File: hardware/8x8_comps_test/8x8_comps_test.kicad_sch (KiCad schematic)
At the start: 10 parts

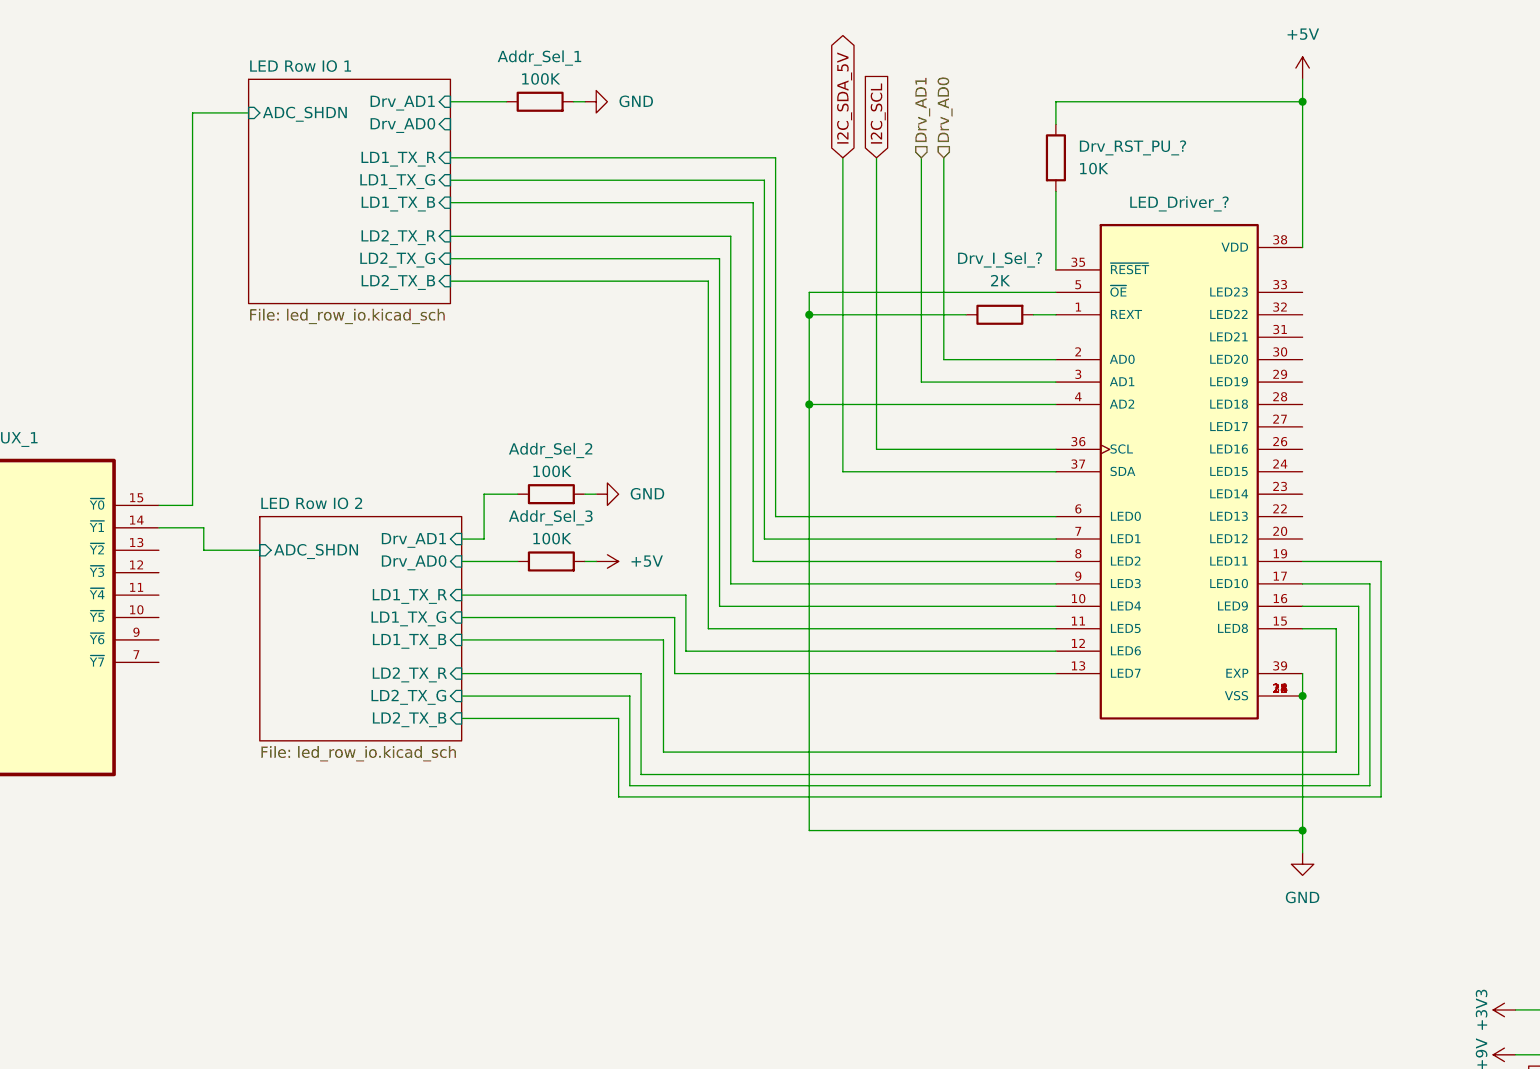
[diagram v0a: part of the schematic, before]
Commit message: Added test Schematic and PCB
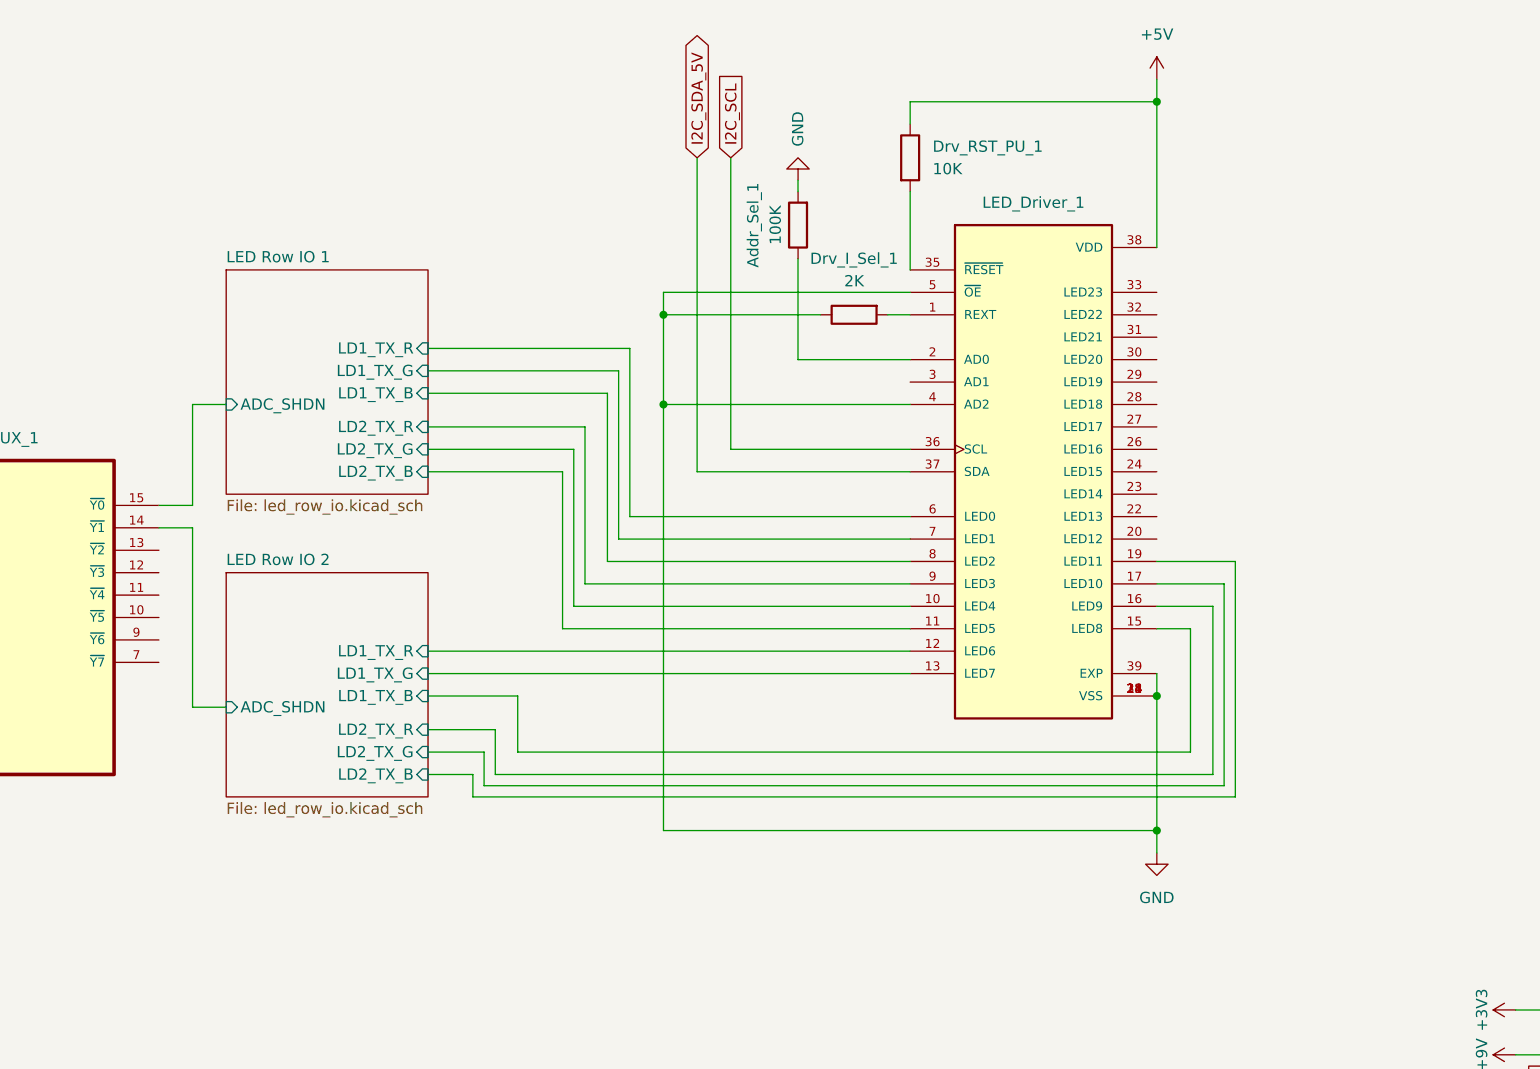
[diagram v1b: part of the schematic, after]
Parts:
- removed Addr_Sel_2, Addr_Sel_3: 100K, Resistor_THT:R_Axial_DIN0207_L6.3mm_D2.5mm_P7.62mm_Horizontal, symbol Device:R
- gave numbers to parts that had none: 3
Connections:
- net LED Row IO 1/Drv_AD1 is gone; now on an unnamed net: Addr_Sel_1.1
- net Drv_AD0: no longer names the net of LED_Driver_1.2 (AD0)
- net Drv_AD1: no longer names the net of LED_Driver_1.3 (AD1)
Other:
- sheet LED Row IO 1 ports: added none; removed Drv_AD0, Drv_AD1
- sheet LED Row IO 2 ports: added none; removed Drv_AD0, Drv_AD1
- moved on the sheet: Addr_Sel_1, Drv_I_Sel_1, Drv_RST_PU_1, LED_Driver_1

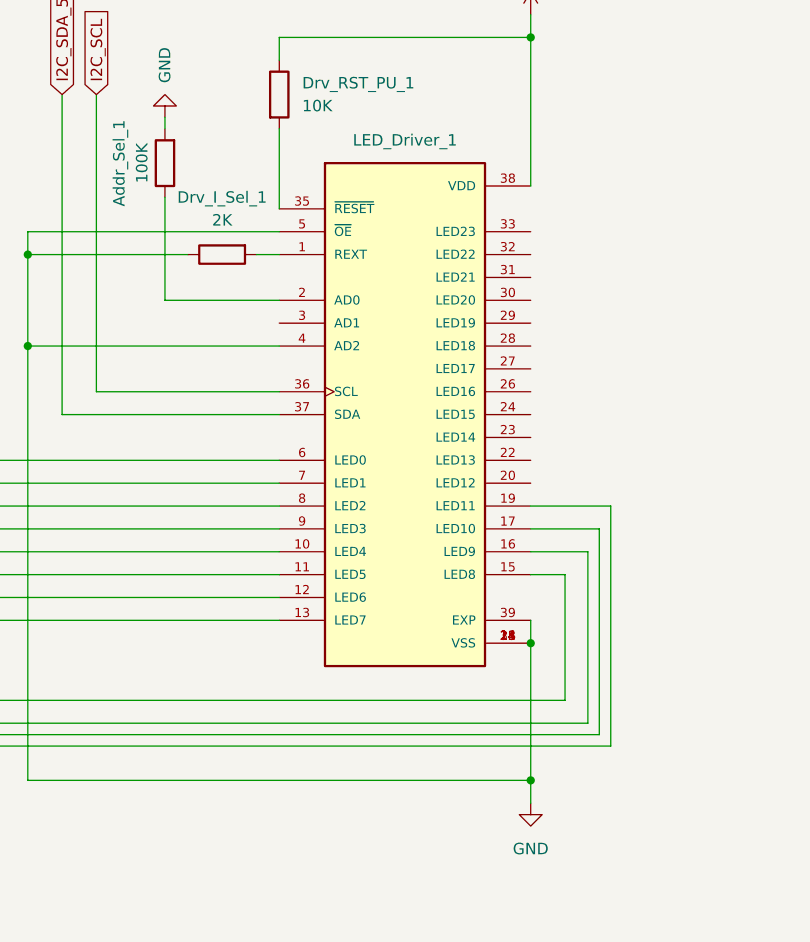
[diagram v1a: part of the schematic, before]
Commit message: Updated Footprints
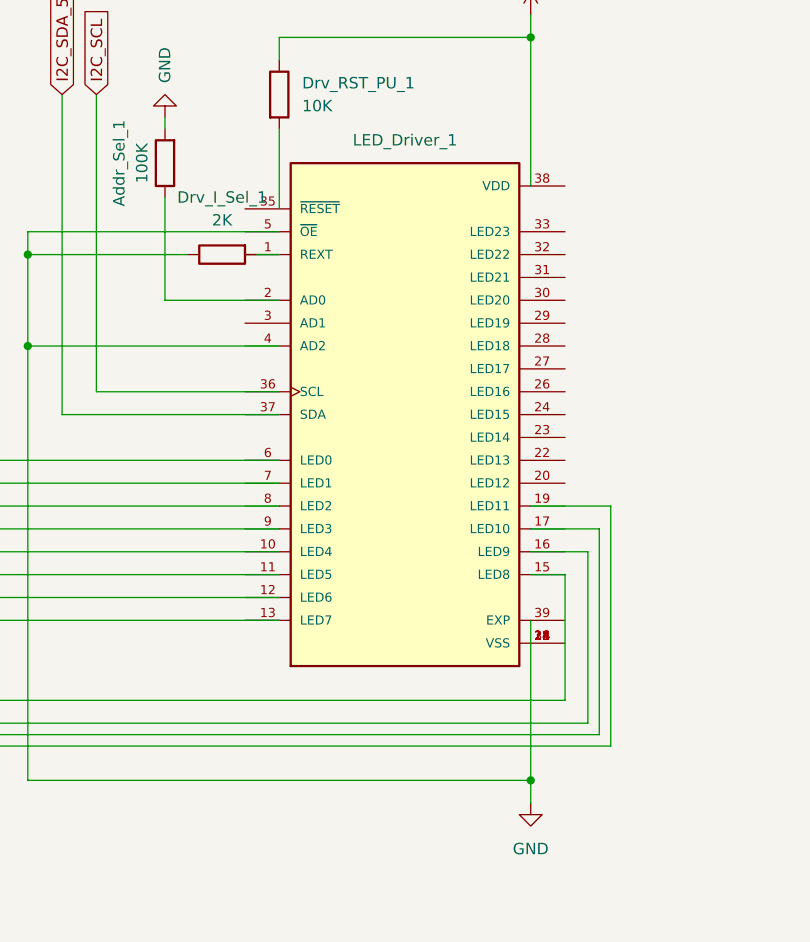
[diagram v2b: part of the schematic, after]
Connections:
- net +5V: no longer LED_Driver_1.38 (VDD)
- net GND: no longer LED_Driver_1.14 (VSS), LED_Driver_1.18 (VSS), LED_Driver_1.21 (VSS), LED_Driver_1.25 (VSS), LED_Driver_1.34 (VSS), LED_Driver_1.39 (EXP), LED_Driver_1.4 (AD2), LED_Driver_1.5 (~{OE})
- net I2C_SCL: no longer LED_Driver_1.36 (SCL)
- net I2C_SDA_5V: no longer LED_Driver_1.37 (SDA)
- net LED Row IO 1/LD1_TX_B: no longer LED_Driver_1.8 (LED2)
- net LED Row IO 1/LD1_TX_G: no longer LED_Driver_1.7 (LED1)
- net LED Row IO 1/LD1_TX_R: no longer LED_Driver_1.6 (LED0)
- net LED Row IO 1/LD2_TX_B: no longer LED_Driver_1.11 (LED5)
- net LED Row IO 1/LD2_TX_G: no longer LED_Driver_1.10 (LED4)
- net LED Row IO 1/LD2_TX_R: no longer LED_Driver_1.9 (LED3)
- net LED Row IO 2/LD1_TX_G: no longer LED_Driver_1.13 (LED7)
- net LED Row IO 2/LD1_TX_R: no longer LED_Driver_1.12 (LED6)
- net LED Row IO 2/LD2_TX_B: no longer LED_Driver_1.19 (LED11)
- net LED Row IO 2/LD2_TX_G: no longer LED_Driver_1.17 (LED10)
- net LED Row IO 2/LD2_TX_R: no longer LED_Driver_1.16 (LED9)
- net at LED_Driver_1.1 (REXT): no longer Drv_I_Sel_1.2
- net at LED_Driver_1.2 (AD0): no longer Addr_Sel_1.1
- net at LED_Driver_1.35 (~{RESET}): no longer Drv_RST_PU_1.2
- new net: LED_Driver_1.14 (VSS), LED_Driver_1.18 (VSS), LED_Driver_1.21 (VSS), LED_Driver_1.25 (VSS), LED_Driver_1.34 (VSS)
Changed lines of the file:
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@@
   (junction (at 185.42 104.14) (diameter 0) (color 0 0 0 0)
   )
-  (junction (at 185.42 88.9) (diameter 0) (color 0 0 0 0)
-  )
   (junction (at 185.42 21.59) (diameter 0) (color 0 0 0 0)
   )
@@
     (stroke (width 0) (type default) (color 0 0 0 0))
   )
-  (wire (pts (xy 185.42 86.36) (xy 185.42 88.9))
+  (wire (pts (xy 185.42 86.36) (xy 185.42 104.14))
     (stroke (width 0) (type default) (color 0 0 0 0))
   )
@@
   )
   (wire (pts (xy 142.24 173.99) (xy 147.32 173.99))
-    (stroke (width 0) (type default) (color 0 0 0 0))
-  )
-  (wire (pts (xy 185.42 88.9) (xy 185.42 104.14))
     (stroke (width 0) (type default) (color 0 0 0 0))
   )
@@
     )
     (path "/2b9feddb-73ad-4c3f-966c-d0bfee978a2a/2474ab10-6d0b-437f-b5ba-e2a34046d77b"
-      (reference "ADC_1") (unit 1) (value "MCU-MCP3008-I/P(DIP16-7.62MM)") (footprint "ADC:MCP3008-I&slash_P")
+      (reference "ADC_1") (unit 1) (value "MCU-MCP3008-I/P(DIP16-7.62MM)") (footprint "")
     )
     (path "/76f6f663-d57c-43de-8eed-15d7ba876e37/2474ab10-6d0b-437f-b5ba-e2a34046d77b"
-      (reference "ADC_2") (unit 1) (value "MCU-MCP3008-I/P(DIP16-7.62MM)") (footprint "ADC:MCP3008-I&slash_P")
+      (reference "ADC_2") (unit 1) (value "MCU-MCP3008-I/P(DIP16-7.62MM)") (footprint "")
     )
     (path "/2b9feddb-73ad-4c3f-966c-d0bfee978a2a/f9f21eee-0144-4db2-984a-a354c52de809/8ece1949-9e43-4ea1-829b-0a66f8ed07b4"
@@
       (reference "Lvl_Sftr_1") (unit 1) (value "LSF0102DCH") (footprint "Level Shifter:LSF0102DCH")
     )
-    (path "/2b9feddb-73ad-4c3f-966c-d0bfee978a2a/eacddf72-1ebc-4818-ab9b-f2596b88ead0"
-      (reference "OC1") (unit 1) (value "CPC1125N") (footprint "Opto-coupler:footprints")
-    )
-    (path "/2b9feddb-73ad-4c3f-966c-d0bfee978a2a/329ee2f2-cf39-4eb7-8530-1e02f5feefbc"
-      (reference "OC2") (unit 1) (value "CPC1125N") (footprint "Opto-coupler:footprints")
-    )
-    (path "/76f6f663-d57c-43de-8eed-15d7ba876e37/eacddf72-1ebc-4818-ab9b-f2596b88ead0"
-      (reference "OC3") (unit 1) (value "CPC1125N") (footprint "Opto-coupler:footprints")
-    )
-    (path "/76f6f663-d57c-43de-8eed-15d7ba876e37/329ee2f2-cf39-4eb7-8530-1e02f5feefbc"
-      (reference "OC4") (unit 1) (value "CPC1125N") (footprint "Opto-coupler:footprints")
-    )
     (path "/9a5af4de-1bec-4945-88d3-5f7acfd363f1"
       (reference "Pin_Header_1") (unit 1) (value "Conn_02x16_Odd_Even") (footprint "Connector_PinHeader_2.54mm:PinHeader_2x16_P2.54mm_Vertical")
@@
       (reference "Rev_Bias_Sel_1") (unit 1) (value "100K") (footprint "Potentiometer_THT:Potentiometer_Runtron_RM-065_Vertical")
     )
-  )
+    (path "/2b9feddb-73ad-4c3f-966c-d0bfee978a2a/eacddf72-1ebc-4818-ab9b-f2596b88ead0"
+      (reference "SSR1") (unit 1) (value "TLP417A-TP-F") (footprint "SSR:footprints")
+    )
+    (path "/2b9feddb-73ad-4c3f-966c-d0bfee978a2a/329ee2f2-cf39-4eb7-8530-1e02f5feefbc"
+      (reference "SSR2") (unit 1) (value "TLP417A-TP-F") (footprint "SSR:footprints")
+    )
+    (path "/76f6f663-d57c-43de-8eed-15d7ba876e37/eacddf72-1ebc-4818-ab9b-f2596b88ead0"
+      (reference "SSR3") (unit 1) (value "TLP417A-TP-F") (footprint "SSR:footprints")
+    )
+    (path "/76f6f663-d57c-43de-8eed-15d7ba876e37/329ee2f2-cf39-4eb7-8530-1e02f5feefbc"
+      (reference "SSR4") (unit 1) (value "TLP417A-TP-F") (footprint "SSR:footprints")
+    )
+  )

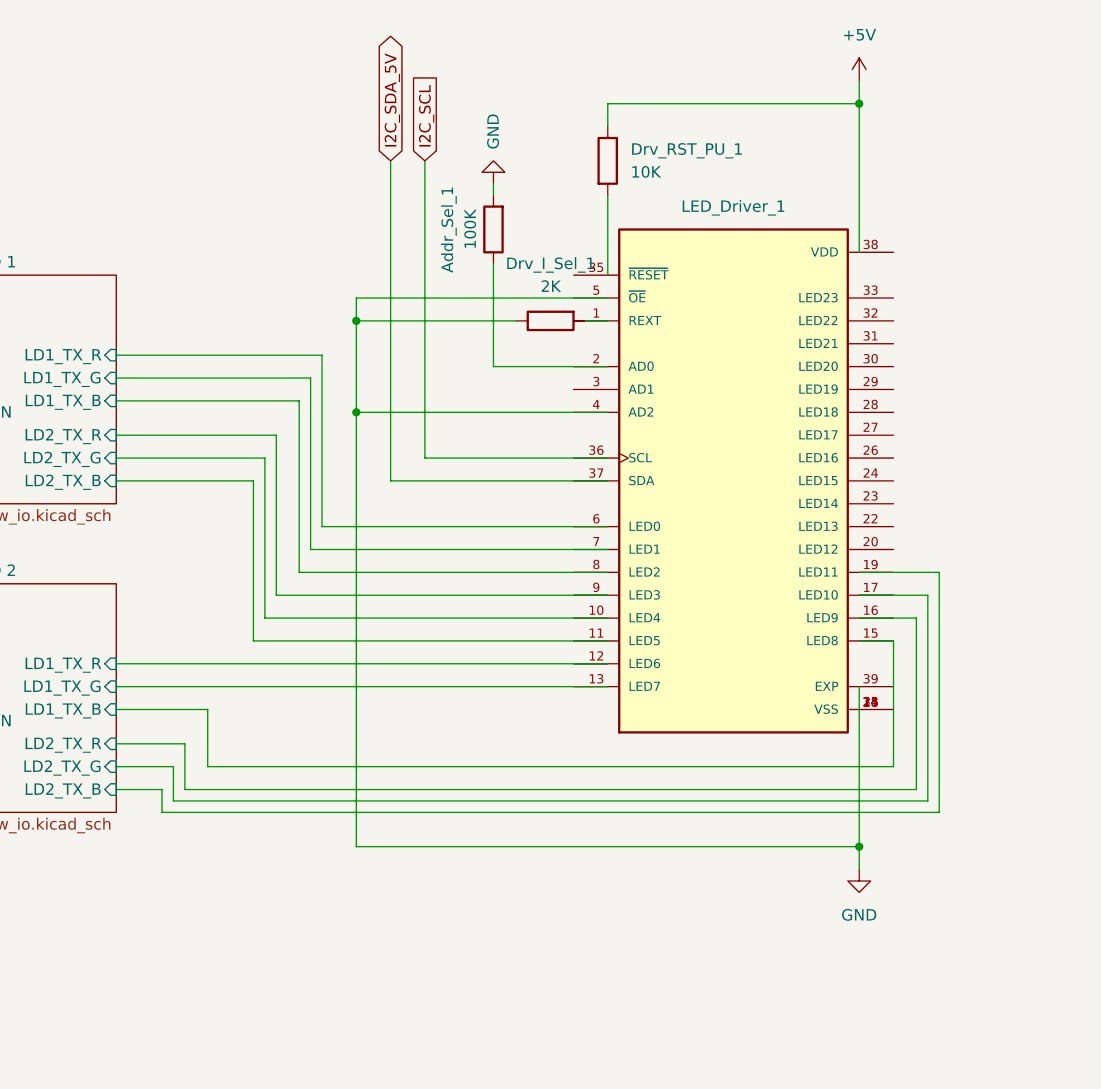
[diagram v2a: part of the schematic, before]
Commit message: Updated Placement
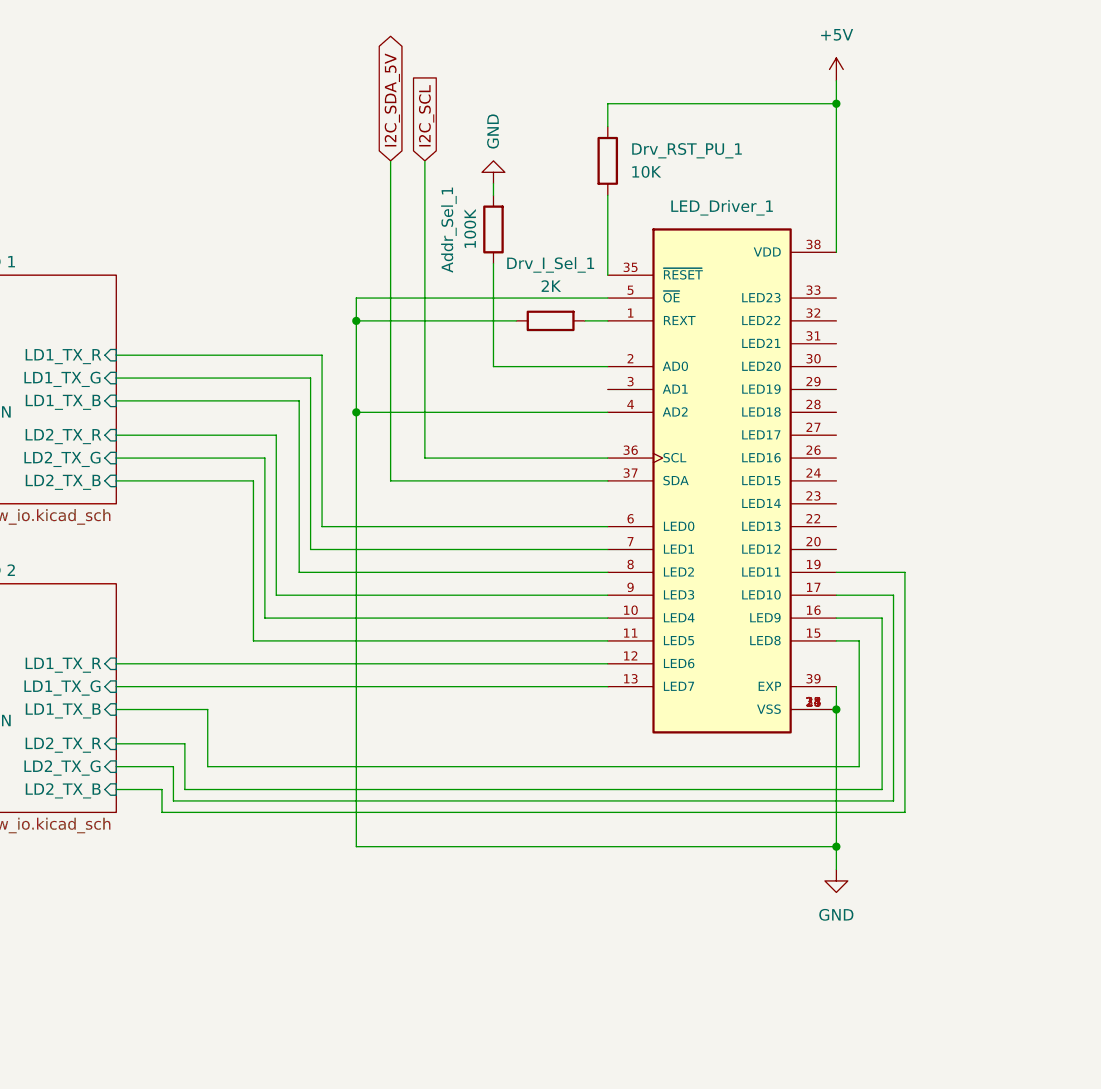
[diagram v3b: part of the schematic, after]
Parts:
- LED_Driver_1: footprint LED Driver:SOP50P640X110-39N -> SOP50P640X110-39N
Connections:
- net +5V: now also LED_Driver_1.38 (VDD)
- net GND: now also LED_Driver_1.14 (VSS), LED_Driver_1.18 (VSS), LED_Driver_1.21 (VSS), LED_Driver_1.25 (VSS), LED_Driver_1.34 (VSS), LED_Driver_1.39 (EXP), LED_Driver_1.4 (AD2), LED_Driver_1.5 (~{OE})
- net I2C_SCL: now also LED_Driver_1.36 (SCL)
- net I2C_SDA_5V: now also LED_Driver_1.37 (SDA)
- net LED Row IO 1/LD1_TX_B: now also LED_Driver_1.8 (LED2)
- net LED Row IO 1/LD1_TX_G: now also LED_Driver_1.7 (LED1)
- net LED Row IO 1/LD1_TX_R: now also LED_Driver_1.6 (LED0)
- net LED Row IO 1/LD2_TX_B: now also LED_Driver_1.11 (LED5)
- net LED Row IO 1/LD2_TX_G: now also LED_Driver_1.10 (LED4)
- net LED Row IO 1/LD2_TX_R: now also LED_Driver_1.9 (LED3)
- net LED Row IO 2/LD1_TX_G: now also LED_Driver_1.13 (LED7)
- net LED Row IO 2/LD1_TX_R: now also LED_Driver_1.12 (LED6)
- net LED Row IO 2/LD2_TX_B: now also LED_Driver_1.19 (LED11)
- net LED Row IO 2/LD2_TX_G: now also LED_Driver_1.17 (LED10)
- net LED Row IO 2/LD2_TX_R: now also LED_Driver_1.16 (LED9)
- net at LED_Driver_1.1 (REXT): now also Drv_I_Sel_1.2
- net at LED_Driver_1.2 (AD0): now also Addr_Sel_1.1
- net at LED_Driver_1.35 (~{RESET}): now also Drv_RST_PU_1.2
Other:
- moved on the sheet: LED_Driver_1
